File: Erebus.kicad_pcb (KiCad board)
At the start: 2 copper layers, 339.1 x 143.2 mm, 382 parts, among them Q1 BSS138, Q2 BSS138, SW1 SW_SPST, SW10 SLSS49E-3, SW11 SLSS49E-3, SW12 SLSS49E-3, SW13 SLSS49E-3, SW14 SLSS49E-3, SW15 SLSS49E-3, SW16 SLSS49E-3, SW17 SLSS49E-3, SW18 SLSS49E-3, SW19 SLSS49E-3, SW2 SLSS49E-3, SW20 SLSS49E-3, SW21 SLSS49E-3, SW22 SLSS49E-3, SW23 SLSS49E-3, SW24 SLSS49E-3, SW25 SLSS49E-3, SW26 SLSS49E-3, SW27 SLSS49E-3, SW28 SLSS49E-3, SW29 SLSS49E-3, SW3 SLSS49E-3, SW30 SLSS49E-3, SW31 SLSS49E-3, SW32 SLSS49E-3, SW33 SLSS49E-3, SW34 SLSS49E-3, SW35 SLSS49E-3, SW36 SLSS49E-3, SW37 SLSS49E-3, SW38 SLSS49E-3, SW39 SLSS49E-3, SW4 SLSS49E-3, SW40 SLSS49E-3, SW41 SLSS49E-3, SW42 SLSS49E-3, SW43 SLSS49E-3, SW44 SLSS49E-3, SW45 SLSS49E-3, SW46 SLSS49E-3, SW47 SLSS49E-3, SW48 SLSS49E-3, SW49 SLSS49E-3, SW5 SLSS49E-3, SW50 SLSS49E-3, SW51 SLSS49E-3, SW52 SLSS49E-3, SW53 SLSS49E-3, SW54 SLSS49E-3, SW55 SLSS49E-3, SW56 SLSS49E-3, SW57 SLSS49E-3, SW58 SLSS49E-3, SW59 SLSS49E-3, SW6 SLSS49E-3, SW60 SLSS49E-3, SW61 SLSS49E-3, SW62 SLSS49E-3, SW63 SLSS49E-3, SW64 SLSS49E-3, SW65 SLSS49E-3, SW66 SLSS49E-3, SW67 SLSS49E-3, SW68 SLSS49E-3, SW69 SLSS49E-3, SW7 SLSS49E-3, SW70 SLSS49E-3, SW71 SLSS49E-3, SW72 SLSS49E-3, SW73 SLSS49E-3, SW74 SLSS49E-3, SW75 SLSS49E-3, SW76 SLSS49E-3, SW77 SLSS49E-3, SW78 SLSS49E-3, SW79 SLSS49E-3, SW8 SLSS49E-3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

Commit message: Switched to split layout ortholinear
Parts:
- removed C1, C169: 10u, Capacitor_SMD:C_0402_1005Metric
- removed C10, C100, C101, C102, C103, C104, C105, C106, C107, C108, C109, C11, C110, C111, C112, C113, C114, C115, C116, C117, C118, C119, C12, C120, C121, C122, C123, C124, C125, C126, C127, C128, C129, C13, C130, C131, C132, C133, C134, C135, C136, C137, C138, C139, C14, C140, C141, C142, C143, C144, C145, C146, C147, C148, C149, C15, C150, C151, C152, C153, C154, C155, C156, C157, C158, C159, C16, C160, C161, C162, C163, C164, C165, C166, C167, C168, C17, C170, C171, C172, C173, C174, C18, C19, C20, C21, C22, C23, C24, C25, C26, C27, C28, C29, C30, C31, C32, C33, C34, C35, C36, C37, C38, C39, C40, C41, C42, C43, C44, C45, C46, C47, C48, C49, C5, C50, C51, C52, C53, C54, C55, C56, C57, C58, C59, C6, C60, C61, C62, C63, C64, C65, C66, C67, C68, C69, C7, C70, C71, C72, C73, C74, C75, C76, C77, C78, C79, C8, C80, C81, C82, C83, C84, C85, C86, C87, C88, C89, C9, C90, C91, C92, C93, C94, C95, C96, C97, C98, C99: 100n, Capacitor_SMD:C_0402_1005Metric
- removed C2: 100u, Capacitor_SMD:C_0402_1005Metric
- removed C3, C4: 22p, Capacitor_SMD:C_0402_1005Metric
- removed ENCODER1: EC11E, PCM_marbastlib-various:ROT_Alps_EC11E-Switch
- removed H1, H2, H3, H4, H5, H6, H7, H8: MountingHole, MountingHole:MountingHole_2.2mm_M2_Pad
- removed Q1, Q2: BSS138, Package_TO_SOT_SMD:SOT-23
- removed R1, R2: 0, Resistor_SMD:R_0603_1608Metric_Pad0.98x0.95mm_HandSolder
- removed R10, R11, R12, R13, R14, R15, R16, R17, R18, R19, R20, R21, R22, R23, R24, R25, R26, R27, R28, R29, R30, R31, R32, R33, R34, R35, R36, R37, R38, R39, R4, R40, R41, R42, R43, R44, R45, R46, R47, R48, R49, R5, R50, R51, R52, R53, R54, R55, R56, R57, R58, R59, R6, R60, R61, R62, R63, R64, R65, R66, R67, R68, R69, R7, R70, R71, R72, R73, R74, R75, R76, R77, R78, R79, R8, R80, R81, R82, R85, R86, R9, R90, R91, R92: 10k, Resistor_SMD:R_0402_1005Metric
- removed R3: 1k5, Resistor_SMD:R_0402_1005Metric
- removed R83: 330k, Resistor_SMD:R_0603_1608Metric
- removed R84: 1M, Resistor_SMD:R_0402_1005Metric
- removed R87: 100k, Resistor_SMD:R_0402_1005Metric
- removed R88: 100, Resistor_SMD:R_0402_1005Metric
- removed R89: 1k, Resistor_SMD:R_0402_1005Metric
- removed S1, S4: MX_stab, PCM_marbastlib-mx:STAB_MX_P_2u
- removed S2, S3: MX_stab, PCM_marbastlib-mx:STAB_MX_P_2.25u
- removed S5: MX_stab, PCM_marbastlib-mx:STAB_MX_P_2.75u
- removed SW28, SW29, SW30, SW31, SW32, SW33, SW34, SW35, SW36, SW37, SW38, SW39, SW40, SW41, SW42, SW43, SW44, SW45, SW46, SW47, SW48, SW49, SW50, SW51, SW52, SW53, SW54, SW55, SW56, SW57, SW58, SW59, SW60, SW61, SW62, SW63, SW64, SW65, SW66, SW67, SW68, SW69, SW70, SW71, SW72, SW73, SW74, SW75, SW76, SW77, SW78, SW79, SW80, SW81, SW82: SLSS49E-3, Erebus:SLSS49E-3 with MX holes
- removed SWD1: Conn_02x03_Odd_Even, Connector_PinHeader_2.54mm:PinHeader_2x03_P2.54mm_Vertical
- removed U10, U11, U6, U7, U8, U9: 74HC4067, Package_SO:TSSOP-24_4.4x7.8mm_P0.65mm
- removed U2, U3: H5VU25U, Erebus:DFN2510
- removed U4: AT32F415CBT7, easyeda2kicad:LQFP-48_L7.0-W7.0-P0.50-LS9.0-BL
- removed U5: STM32F303CBTx, Package_QFP:LQFP-48_7x7mm_P0.5mm
- removed USB1: X1224WRS-04-LPV01, Erebus:PicoEZMate-Reinforced-Alt
- removed Y1: 8MHz, Crystal:Crystal_SMD_3225-4Pin_3.2x2.5mm
- added BT1: JST Connector, KLOR:JST_PH_reversible, F.Cu at (82.3, 104.8)
- added BT2: Battery_Cell, KLOR:custombatteryconnector_small, F.Cu at (82.5, 113.2)
- added D10: D_Small, KLOR:Diode_SOD123, F.Cu at (193.6, 111.0)
- added D11: D_Small, KLOR:Diode_SOD123, F.Cu at (221.9, 110.9)
- added D12: D_Small, KLOR:Diode_SOD123, F.Cu at (116.8, 118.3)
- added D13: D_Small, KLOR:Diode_SOD123, F.Cu at (148.2, 103.2)
- added D14: D_Small, KLOR:Diode_SOD123, F.Cu at (155.0, 106.3)
- added D15: D_Small, KLOR:Diode_SOD123, F.Cu at (174.6, 116.3)
- added D16: D_Small, KLOR:Diode_SOD123, F.Cu at (190.3, 129.7)
- added D17: D_Small, KLOR:Diode_SOD123, F.Cu at (218.5, 129.5)
- added D18: D_Small, KLOR:Diode_SOD123, F.Cu at (100.9, 107.0)
- added D19: D_Small, KLOR:Diode_SOD123, F.Cu at (88.3, 143.7)
- added D2: D_Small, KLOR:Diode_SOD123, F.Cu at (136.0, 77.1)
- added D20: D_Small, KLOR:Diode_SOD123, F.Cu at (107.5, 131.9)
- added D21: D_Small, KLOR:Diode_SOD123, F.Cu at (129.1, 125.2)
- added D22: D_Small, KLOR:Diode_SOD123, F.Cu at (151.6, 124.3)
- added D3: D_Small, KLOR:Diode_SOD123, F.Cu at (155.1, 68.1)
- added D4: D_Small, KLOR:Diode_SOD123, F.Cu at (176.0, 78.2)
- added D5: D_Small, KLOR:Diode_SOD123, F.Cu at (196.9, 92.2)
- added D6: D_Small, KLOR:Diode_SOD123, F.Cu at (117.0, 99.2)
- added D7: D_Small, KLOR:Diode_SOD123, F.Cu at (137.0, 96.2)
- added D8: D_Small, KLOR:Diode_SOD123, F.Cu at (155.1, 87.2)
- added D9: D_Small, KLOR:Diode_SOD123, F.Cu at (174.6, 97.3)
- added J1: MJ-4PP-9, KLOR:MJ-4PP-9, F.Cu at (80.9, 127.4)
- added JP22: Device_Jumper_NO_Small, KLOR:Jumper, F.Cu at (81.9, 108.5)
- added JP23: Device_Jumper_NO_Small, KLOR:Jumper, B.Cu at (83.7, 108.5)
- added JP24: Device_Jumper_NO_Small, KLOR:Jumper, F.Cu at (83.7, 108.5)
- added JP25: Device_Jumper_NO_Small, KLOR:Jumper, B.Cu at (81.9, 108.5)
- added JP26: Device_Jumper_NO_Small, KLOR:Jumper, B.Cu at (91.0, 136.6)
- added JP3: Device_Jumper_NO_Small, KLOR:Jumper, F.Cu at (95.2, 101.8)
- added JP4: Device_Jumper_NO_Small, KLOR:Jumper, F.Cu at (92.6, 101.8)
- added JP5: Device_Jumper_NO_Small, KLOR:Jumper, B.Cu at (100.2, 101.8)
- added JP6: Device_Jumper_NO_Small, KLOR:Jumper, B.Cu at (97.7, 101.8)
- added JP7: Device_Jumper_NO_Small, KLOR:Jumper, B.Cu at (95.2, 101.8)
- added JP8: Device_Jumper_NO_Small, KLOR:Jumper, B.Cu at (92.6, 101.8)
- added MH1: MountingHole_3.2mm_M3, MountingHole:MountingHole_3.2mm_M3, F.Cu at (83.3, 36.6)
- added MH2: MountingHole_3.2mm_M3, MountingHole:MountingHole_3.2mm_M3, F.Cu at (145.4, 36.6)
- added MH3: MountingHole_3.2mm_M3, MountingHole:MountingHole_3.2mm_M3, F.Cu at (175.5, 36.7)
- added MH4: MountingHole_3.2mm_M3, MountingHole:MountingHole_3.2mm_M3, F.Cu at (190.3, 37.7)
- added MH5: MountingHole_3.2mm_M3, MountingHole:MountingHole_3.2mm_M3, F.Cu at (167.3, 88.0)
- added MH6: MountingHole_3.2mm_M3, MountingHole:MountingHole_3.2mm_M3, F.Cu at (83.3, 135.2)
- added MH7: MountingHole_3.2mm_M3, MountingHole:MountingHole_3.2mm_M3, F.Cu at (169.9, 121.7)
- added MH8: MountingHole_3.2mm_M3, MountingHole:MountingHole_3.2mm_M3, F.Cu at (181.6, 122.5)
- added MH9: MountingHole_2.2mm_M2, MountingHole:MountingHole_2.2mm_M2, F.Cu at (196.6, 56.3)
- added PSW1: SW_DPDT_x2, KLOR:MSK12C02_reversible, F.Cu at (80.9, 41.1)
- added RSW1: SW_Push, KLOR:SW_Push_1P1T-MP_NO_Horizontal_Alps_SKRTLAE010_both_sides, F.Cu at (82.3, 120.7)
- D1: value 1N4148WS -> D_Small; footprint Diode_SMD:D_SOD-323 -> KLOR:Diode_SOD123
- JP1, JP2: value Jumper_2_Open -> Device_Jumper_NO_Small; footprint Connector_PinHeader_2.54mm:PinHeader_1x02_P2.54mm_Vertical -> KLOR:Jumper
- OLED1: value Conn_01x04_Socket -> SSD1306; footprint Erebus:OLED Module -> KLOR:SSD1306_128x64OLED
- SW1: value SW_SPST -> SW_PUSH-MX_W_LED; footprint Button_Switch_SMD:SW_SPST_TL3342 -> KLOR:SK6812MINI_and_cherry; moved to F.Cu
- SW10, SW11, SW12, SW13, SW14, SW15, SW16, SW17, SW19, SW2, SW20, SW21, SW22, SW23, SW24, SW25, SW26, SW27, SW3, SW4, SW5, SW6, SW7, SW8, SW9: value SLSS49E-3 -> SW_PUSH-MX_W_LED; footprint Erebus:SLSS49E-3 with MX holes -> KLOR:SK6812MINI_and_cherry; moved to F.Cu
- SW18: value SLSS49E-3 -> RotaryEncoder_Switch; footprint Erebus:SLSS49E-3 with MX holes -> KLOR:RotaryEncoder_Alps_EC11E-Switch_Vertical_H20mm-keebio_modified; moved to F.Cu
- U1: value AMS1117-3.3 -> ProMicro; footprint Package_TO_SOT_SMD:SOT-223-3_TabPin2 -> KLOR:ProMicro
- moved D1 293.0 mm to (117.0, 80.1)
- moved U1 293.0 mm to (97.6, 52.5)
- moved SW15 185.5 mm to (178.2, 108.1), turned to 176 degrees
- moved SW13 154.8 mm to (140.1, 106.7)
- moved SW12 153.3 mm to (121.1, 109.7), turned to 180 degrees
- moved SW16 151.8 mm to (196.1, 122.1), turned to 170 degrees
- moved SW17 151.7 mm to (215.7, 120.5), turned to 170 degrees
- moved SW14 151.1 mm to (159.1, 97.7)
- moved SW5 102.6 mm to (202.7, 84.5), turned to 170 degrees
- moved SW2 98.4 mm to (140.1, 68.6)
- moved SW4 97.2 mm to (180.9, 70.0), turned to 176 degrees
- moved SW3 91.7 mm to (159.1, 59.6)
- moved SW19 90.9 mm to (85.4, 152.9), turned to -135 degrees
- moved OLED1 89.1 mm to (96.6, 87.9), turned to 180 degrees
- moved JP2 83.3 mm to (97.7, 101.8), turned to -90 degrees
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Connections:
- D1 pad 1: Net-(D1-K) -> row0
- D1 pad 2: /reset/switch -> Net-(D1-A)
- JP1 pad 1: GND -> Net-(OLED1-GND)
- JP1 pad 2: /~{RESET} -> GND
- JP2 pad 1: +3V3 -> Net-(OLED1-VCC)
- JP2 pad 2: /BOOT0 -> VCC
- OLED1 pad 1: GND -> Net-(OLED1-GND)
- OLED1 pad 2: +3V3 -> Net-(OLED1-VCC)
- OLED1 pad 3: /I2C1_SCL -> Net-(OLED1-SCL)
- OLED1 pad 4: /I2C1_SDA -> Net-(OLED1-SDA)
- SW1 pad 1: +3V3 -> Net-(SW1B-DOUT)
- SW1 pad 2: /reset/switch -> GND
- SW10 pad 1: +3V3 -> Net-(SW10B-DOUT)
- SW10 pad 3: Net-(SW10-VOUT) -> Net-(SW10B-DIN)
- SW11 pad 1: +3V3 -> Net-(SW11B-DOUT)
- SW11 pad 3: Net-(SW11-VOUT) -> Net-(SW11B-DIN)
- SW12 pad 1: +3V3 -> Net-(SW12B-DOUT)
- SW12 pad 3: Net-(SW12-VOUT) -> Net-(SW12B-DIN)
- SW13 pad 1: +3V3 -> Net-(SW13B-DOUT)
- SW13 pad 3: Net-(SW13-VOUT) -> Net-(SW13B-DIN)
- SW14 pad 1: +3V3 -> Net-(SW14B-DOUT)
- SW14 pad 3: Net-(SW14-VOUT) -> Net-(SW14B-DIN)
- SW15 pad 1: +3V3 -> Net-(SW15B-DOUT)
- SW15 pad 3: Net-(SW15-VOUT) -> Net-(SW15B-DIN)
- SW16 pad 1: +3V3 -> Net-(SW10B-DIN)
- SW16 pad 3: Net-(SW16-VOUT) -> Net-(SW15B-DOUT)
- SW17 pad 1: +3V3 -> unconnected-(SW17B-DOUT-Pad1)
- SW17 pad 3: Net-(SW17-VOUT) -> Net-(SW11B-DOUT)
- SW19 pad 1: +3V3 -> Net-(SW19B-DOUT)
- SW19 pad 3: Net-(SW19-VOUT) -> LED
- SW2 pad 1: +3V3 -> Net-(SW2B-DOUT)
- SW2 pad 3: Net-(SW2-VOUT) -> Net-(SW1B-DOUT)
- SW20 pad 1: +3V3 -> Net-(SW20B-DOUT)
- SW20 pad 3: Net-(SW20-VOUT) -> Net-(SW19B-DOUT)
- SW21 pad 1: +3V3 -> Net-(SW12B-DIN)
- SW21 pad 3: Net-(SW21-VOUT) -> Net-(SW20B-DOUT)
- SW22 pad 1: +3V3 -> Net-(SW14B-DIN)
- SW22 pad 3: Net-(SW22-VOUT) -> Net-(SW13B-DOUT)
- SW23 pad 1: +3V3 -> (no net)
- SW23 pad 2: GND -> (no net)
- SW23 pad 3: Net-(SW23-VOUT) -> (no net)
- SW24 pad 1: +3V3 -> (no net)
- SW24 pad 2: GND -> (no net)
- SW24 pad 3: Net-(SW24-VOUT) -> (no net)
- SW25 pad 1: +3V3 -> (no net)
- SW25 pad 2: GND -> (no net)
- SW25 pad 3: Net-(SW25-VOUT) -> (no net)
- SW26 pad 1: +3V3 -> (no net)
- SW26 pad 2: GND -> (no net)
- SW26 pad 3: Net-(SW26-VOUT) -> (no net)
- SW27 pad 1: +3V3 -> (no net)
- SW27 pad 2: GND -> (no net)
- SW27 pad 3: Net-(SW27-VOUT) -> (no net)
- SW3 pad 1: +3V3 -> Net-(SW3B-DOUT)
- SW3 pad 3: Net-(SW3-VOUT) -> Net-(SW3B-DIN)
- SW4 pad 1: +3V3 -> Net-(SW4B-DOUT)
- SW4 pad 3: Net-(SW4-VOUT) -> Net-(SW3B-DOUT)
- SW5 pad 1: +3V3 -> Net-(SW11B-DIN)
- SW5 pad 3: Net-(SW5-VOUT) -> Net-(SW10B-DOUT)
- SW6 pad 1: +3V3 -> Net-(SW1B-DIN)
- SW6 pad 3: Net-(SW6-VOUT) -> Net-(SW12B-DOUT)
- SW7 pad 1: +3V3 -> Net-(SW13B-DIN)
- SW7 pad 3: Net-(SW7-VOUT) -> Net-(SW2B-DOUT)
- SW8 pad 1: +3V3 -> Net-(SW3B-DIN)
- SW8 pad 3: Net-(SW8-VOUT) -> Net-(SW14B-DOUT)
- SW9 pad 1: +3V3 -> Net-(SW15B-DIN)
- SW9 pad 3: Net-(SW9-VOUT) -> Net-(SW4B-DOUT)
- U1 pad 1: GND -> LED
- U1 pad 2: +3V3 -> TX
- U1 pad 3: +5V -> GND
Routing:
- net GND: track 343.4 -> 0.00 mm, vias 248 -> 0
- net /S0: track 290.4 -> 0.00 mm
- net /S2: track 287.0 -> 0.00 mm
- net /S1: track 286.8 -> 0.00 mm
- net /S3: track 279.9 -> 0.00 mm
- net /ENCODER_B: track 182.5 -> 0.00 mm
- net /ENCODER_A: track 176.6 -> 0.00 mm
- net /ENCODER_SW: track 173.4 -> 0.00 mm
- net /ADC1_IN3: track 149.6 -> 0.00 mm
- net +3V3: track 110.1 -> 0.00 mm
- net /multiplexers/keys/KEYS_0_13: track 88.7 -> 0.00 mm, vias 2 -> 0
- net /multiplexers/keys/KEYS_0_10: track 82.9 -> 0.00 mm, vias 2 -> 0
- net /multiplexers/keys/KEYS_0_12: track 79.2 -> 0.00 mm, vias 2 -> 0
- net /multiplexers/keys/KEYS_0_8: track 79.0 -> 0.00 mm, vias 2 -> 0
- net /multiplexers/keys/KEYS_0_2: track 73.0 -> 0.00 mm, vias 2 -> 0
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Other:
- board size 339.1 x 143.2 mm -> 160 x 137.3 mm
- rule pad_to_mask_clearance: 0.038 -> 0
- board text added: "--AUDIO"
- board text added: "--GND"
- board text added: "--LED"
- board text added: "--ROW0"
- board text added: "--ROW1"
- board text added: "--ROW2"
- board text added: "--ROW3"
- board text added: "--RX"
- board text added: "--SCL"
- board text added: "--SDA"
- board text added: "--TX"
- board text added: "BATT"
- board text added: "BATT+--"
- board text added: "BLK"
- board text added: "COL0--"
- board text added: "COL1--"
- board text added: "COL2--"
- board text added: "COL3--"
- board text added: "COL4--"
- board text added: "COL5--"
- board text added: "ENC"
- board text added: "ENC A--"
- board text added: "ENC B--"
- board text added: "GND"
- board text added: "GND--"
- board text added: "LOST THUMB?"
- board text added: "MOUNT MCU ON BOTTOM COMPONENTS FACING PCB"
- board text added: "OLED"
- board text added: "RED"
- board text added: "RST"
- board text added: "RST--"
- board text added: "SCL"
- board text added: "SDA"
- board text added: "TENTING PUCK"
- board text added: "TRACK BALL"
- board text added: "VCC"
- board text added: "VCC--"

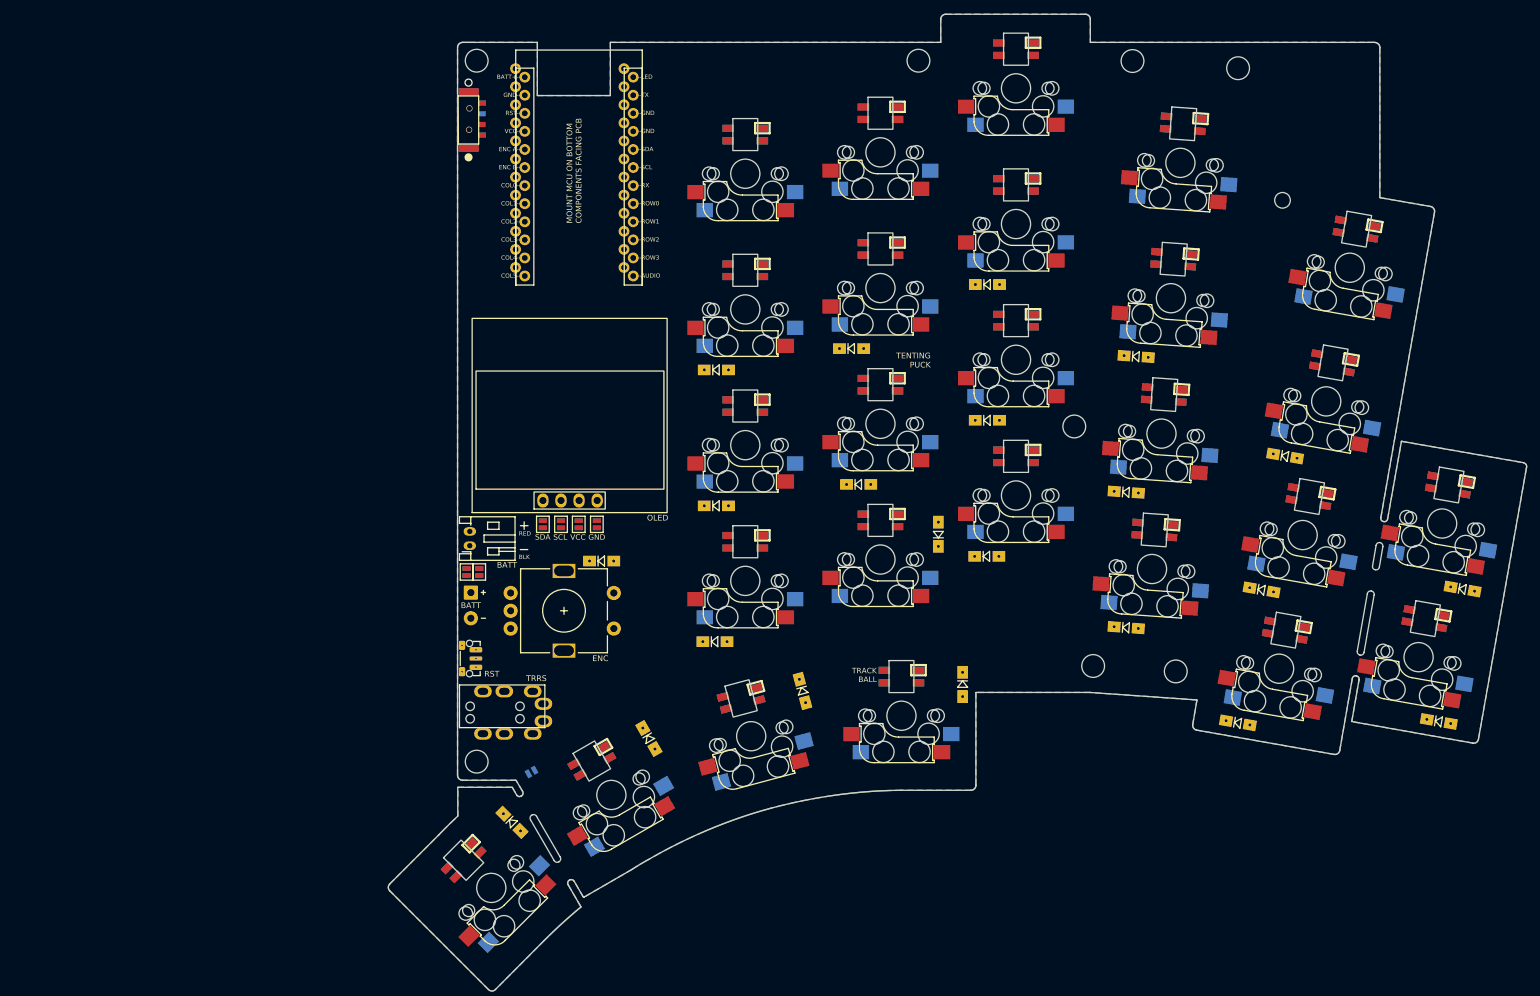
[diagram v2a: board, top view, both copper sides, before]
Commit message: Added and finalized layout of switches
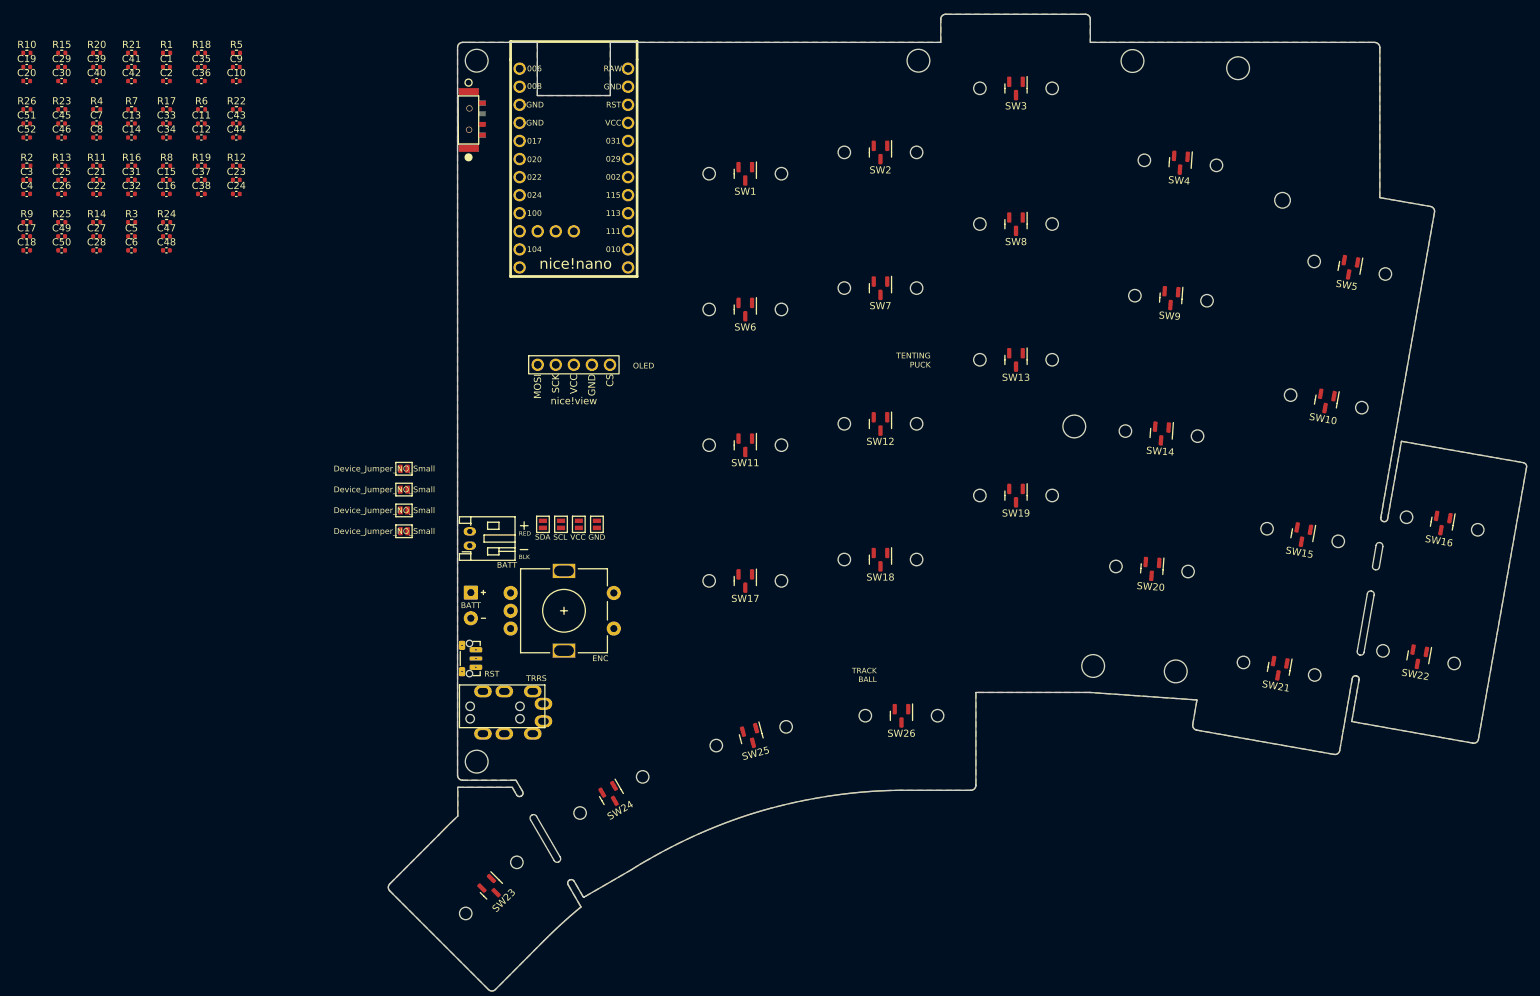
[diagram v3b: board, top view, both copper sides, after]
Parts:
- removed D1, D10, D11, D12, D13, D14, D15, D16, D17, D18, D19, D2, D20, D21, D22, D3, D4, D5, D6, D7, D8, D9: D_Small, KLOR:Diode_SOD123
- removed JP22, JP23, JP24, JP25, JP26: Device_Jumper_NO_Small, KLOR:Jumper
- removed OLED1: SSD1306, KLOR:SSD1306_128x64OLED
- removed SW27: SW_PUSH-MX_W_LED, KLOR:SK6812MINI_and_cherry
- added C1: 100n, Capacitor_SMD:C_0402_1005Metric, F.Cu at (39.7, 37.5)
- added C10: 100n, Capacitor_SMD:C_0402_1005Metric, F.Cu at (49.5, 39.5)
- added C11: 100n, Capacitor_SMD:C_0402_1005Metric, F.Cu at (44.6, 45.5)
- added C12: 100n, Capacitor_SMD:C_0402_1005Metric, F.Cu at (44.6, 47.4)
- added C13: 100n, Capacitor_SMD:C_0402_1005Metric, F.Cu at (34.8, 45.5)
- added C14: 100n, Capacitor_SMD:C_0402_1005Metric, F.Cu at (34.8, 47.4)
- added C15: 100n, Capacitor_SMD:C_0402_1005Metric, F.Cu at (39.7, 53.4)
- added C16: 100n, Capacitor_SMD:C_0402_1005Metric, F.Cu at (39.7, 55.4)
- added C17: 100n, Capacitor_SMD:C_0402_1005Metric, F.Cu at (20.1, 61.3)
- added C18: 100n, Capacitor_SMD:C_0402_1005Metric, F.Cu at (20.1, 63.3)
- added C19: 100n, Capacitor_SMD:C_0402_1005Metric, F.Cu at (20.1, 37.5)
- added C2: 100n, Capacitor_SMD:C_0402_1005Metric, F.Cu at (39.7, 39.5)
- added C20: 100n, Capacitor_SMD:C_0402_1005Metric, F.Cu at (20.1, 39.5)
- added C21: 100n, Capacitor_SMD:C_0402_1005Metric, F.Cu at (29.9, 53.4)
- added C22: 100n, Capacitor_SMD:C_0402_1005Metric, F.Cu at (29.9, 55.4)
- added C23: 100n, Capacitor_SMD:C_0402_1005Metric, F.Cu at (49.5, 53.4)
- added C24: 100n, Capacitor_SMD:C_0402_1005Metric, F.Cu at (49.5, 55.4)
- added C25: 100n, Capacitor_SMD:C_0402_1005Metric, F.Cu at (25.0, 53.4)
- added C26: 100n, Capacitor_SMD:C_0402_1005Metric, F.Cu at (25.0, 55.4)
- added C27: 100n, Capacitor_SMD:C_0402_1005Metric, F.Cu at (29.9, 61.3)
- added C28: 100n, Capacitor_SMD:C_0402_1005Metric, F.Cu at (29.9, 63.3)
- added C29: 100n, Capacitor_SMD:C_0402_1005Metric, F.Cu at (25.0, 37.5)
- added C3: 100n, Capacitor_SMD:C_0402_1005Metric, F.Cu at (20.1, 53.4)
- added C30: 100n, Capacitor_SMD:C_0402_1005Metric, F.Cu at (25.0, 39.5)
- added C31: 100n, Capacitor_SMD:C_0402_1005Metric, F.Cu at (34.8, 53.4)
- added C32: 100n, Capacitor_SMD:C_0402_1005Metric, F.Cu at (34.8, 55.4)
- added C33: 100n, Capacitor_SMD:C_0402_1005Metric, F.Cu at (39.7, 45.5)
- added C34: 100n, Capacitor_SMD:C_0402_1005Metric, F.Cu at (39.7, 47.4)
- added C35: 100n, Capacitor_SMD:C_0402_1005Metric, F.Cu at (44.6, 37.5)
- added C36: 100n, Capacitor_SMD:C_0402_1005Metric, F.Cu at (44.6, 39.5)
- added C37: 100n, Capacitor_SMD:C_0402_1005Metric, F.Cu at (44.6, 53.4)
- added C38: 100n, Capacitor_SMD:C_0402_1005Metric, F.Cu at (44.6, 55.4)
- added C39: 100n, Capacitor_SMD:C_0402_1005Metric, F.Cu at (29.9, 37.5)
- added C4: 100n, Capacitor_SMD:C_0402_1005Metric, F.Cu at (20.1, 55.4)
- added C40: 100n, Capacitor_SMD:C_0402_1005Metric, F.Cu at (29.9, 39.5)
- added C41: 100n, Capacitor_SMD:C_0402_1005Metric, F.Cu at (34.8, 37.5)
- added C42: 100n, Capacitor_SMD:C_0402_1005Metric, F.Cu at (34.8, 39.5)
- added C43: 100n, Capacitor_SMD:C_0402_1005Metric, F.Cu at (49.5, 45.5)
- added C44: 100n, Capacitor_SMD:C_0402_1005Metric, F.Cu at (49.5, 47.4)
- added C45: 100n, Capacitor_SMD:C_0402_1005Metric, F.Cu at (25.0, 45.5)
- added C46: 100n, Capacitor_SMD:C_0402_1005Metric, F.Cu at (25.0, 47.4)
- added C47: 100n, Capacitor_SMD:C_0402_1005Metric, F.Cu at (39.7, 61.3)
- added C48: 100n, Capacitor_SMD:C_0402_1005Metric, F.Cu at (39.7, 63.3)
- added C49: 100n, Capacitor_SMD:C_0402_1005Metric, F.Cu at (25.0, 61.3)
- added C5: 100n, Capacitor_SMD:C_0402_1005Metric, F.Cu at (34.8, 61.3)
- added C50: 100n, Capacitor_SMD:C_0402_1005Metric, F.Cu at (25.0, 63.3)
- added C51: 100n, Capacitor_SMD:C_0402_1005Metric, F.Cu at (20.1, 45.5)
- added C52: 100n, Capacitor_SMD:C_0402_1005Metric, F.Cu at (20.1, 47.4)
- added C6: 100n, Capacitor_SMD:C_0402_1005Metric, F.Cu at (34.8, 63.3)
- added C7: 100n, Capacitor_SMD:C_0402_1005Metric, F.Cu at (29.9, 45.5)
- added C8: 100n, Capacitor_SMD:C_0402_1005Metric, F.Cu at (29.9, 47.4)
- added C9: 100n, Capacitor_SMD:C_0402_1005Metric, F.Cu at (49.5, 37.5)
- added Display1: nice!view, EREBUS:nice_view, F.Cu at (97.0, 62.9)
- added ENCODER1: RotaryEncoder_Switch, EREBUS:RotaryEncoder_Alps_EC11E-Switch_Vertical_H20mm-keebio_modified, F.Cu at (95.6, 114.0)
- added R1: 10k, Resistor_SMD:R_0402_1005Metric, F.Cu at (39.7, 35.6)
- added R10: 10k, Resistor_SMD:R_0402_1005Metric, F.Cu at (20.1, 35.6)
- added R11: 10k, Resistor_SMD:R_0402_1005Metric, F.Cu at (29.9, 51.4)
- added R12: 10k, Resistor_SMD:R_0402_1005Metric, F.Cu at (49.6, 51.4)
- added R13: 10k, Resistor_SMD:R_0402_1005Metric, F.Cu at (25.0, 51.4)
- added R14: 10k, Resistor_SMD:R_0402_1005Metric, F.Cu at (29.9, 59.4)
- added R15: 10k, Resistor_SMD:R_0402_1005Metric, F.Cu at (25.0, 35.6)
- added R16: 10k, Resistor_SMD:R_0402_1005Metric, F.Cu at (34.8, 51.4)
- added R17: 10k, Resistor_SMD:R_0402_1005Metric, F.Cu at (39.7, 43.5)
- added R18: 10k, Resistor_SMD:R_0402_1005Metric, F.Cu at (44.6, 35.6)
- added R19: 10k, Resistor_SMD:R_0402_1005Metric, F.Cu at (44.6, 51.4)
- added R2: 10k, Resistor_SMD:R_0402_1005Metric, F.Cu at (20.1, 51.4)
- added R20: 10k, Resistor_SMD:R_0402_1005Metric, F.Cu at (29.9, 35.6)
- added R21: 10k, Resistor_SMD:R_0402_1005Metric, F.Cu at (34.8, 35.6)
- added R22: 10k, Resistor_SMD:R_0402_1005Metric, F.Cu at (49.6, 43.5)
- added R23: 10k, Resistor_SMD:R_0402_1005Metric, F.Cu at (25.0, 43.5)
- added R24: 10k, Resistor_SMD:R_0402_1005Metric, F.Cu at (39.7, 59.4)
- added R25: 10k, Resistor_SMD:R_0402_1005Metric, F.Cu at (25.0, 59.4)
- added R26: 10k, Resistor_SMD:R_0402_1005Metric, F.Cu at (20.1, 43.5)
- added R3: 10k, Resistor_SMD:R_0402_1005Metric, F.Cu at (34.8, 59.4)
- added R4: 10k, Resistor_SMD:R_0402_1005Metric, F.Cu at (29.9, 43.5)
- added R5: 10k, Resistor_SMD:R_0402_1005Metric, F.Cu at (49.6, 35.6)
- added R6: 10k, Resistor_SMD:R_0402_1005Metric, F.Cu at (44.6, 43.5)
- added R7: 10k, Resistor_SMD:R_0402_1005Metric, F.Cu at (34.8, 43.5)
- added R8: 10k, Resistor_SMD:R_0402_1005Metric, F.Cu at (39.7, 51.4)
- added R9: 10k, Resistor_SMD:R_0402_1005Metric, F.Cu at (20.1, 59.4)
- BT1: value JST Connector -> Battery_Cell
- BT2: value Battery_Cell -> JST Connector
- JP1, JP2, JP3, JP4: footprint KLOR:Jumper -> EREBUS:Jumper
- JP5, JP6, JP7, JP8: moved to F.Cu
- SW1, SW10, SW11, SW12, SW13, SW14, SW15, SW16, SW17, SW19, SW2, SW20, SW21, SW22, SW23, SW24, SW25, SW26, SW3, SW4, SW5, SW6, SW7, SW8, SW9: value SW_PUSH-MX_W_LED -> SLSS49E-3; footprint KLOR:SK6812MINI_and_cherry -> EREBUS:SLSS49E-3 with MX holes
- SW18: value RotaryEncoder_Switch -> SLSS49E-3; footprint KLOR:RotaryEncoder_Alps_EC11E-Switch_Vertical_H20mm-keebio_modified -> EREBUS:SLSS49E-3 with MX holes
- U1: value ProMicro -> nice_nano; footprint KLOR:ProMicro -> EREBUS:nice_nano
- moved SW23 106.5 mm to (85.4, 152.9), turned to 45 degrees
- moved SW11 98.5 mm to (121.1, 90.7), turned to 0 degrees
- moved SW25 98.4 mm to (121.9, 131.6), turned to 15 degrees
- moved SW24 97.9 mm to (102.2, 139.8), turned to 30 degrees
- moved SW17 95.2 mm to (121.1, 109.7), turned to 0 degrees
- moved SW19 92.1 mm to (159.1, 97.7), turned to 0 degrees
- moved SW26 87.0 mm to (143.0, 128.7), turned to 0 degrees
- moved SW20 82.3 mm to (178.2, 108.1), turned to -4 degrees
- moved SW21 74.8 mm to (196.1, 122.1), turned to -10 degrees
- moved SW22 73.1 mm to (215.7, 120.5), turned to -10 degrees
- moved SW18 45.1 mm to (140.1, 106.7)
- moved SW13 33.9 mm to (159.1, 78.7), turned to 0 degrees
- moved SW16 30.7 mm to (219.0, 101.7), turned to -10 degrees
- moved SW12 29.1 mm to (140.1, 87.7), turned to 0 degrees
- moved JP1 28.2 mm to (73.1, 94.0), turned to 0 degrees
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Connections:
- BT1 pad 1: /PAD1 -> /PSW
- BT1 pad 2: /PAD2 -> GND
- BT2 pad 1: /PSW -> /PAD1
- BT2 pad 2: GND -> /PAD2
- JP1 pad 1: Net-(OLED1-GND) -> /PAD2
- JP1 pad 2: GND -> /PSW
- JP2 pad 1: Net-(OLED1-VCC) -> /PAD2
- JP2 pad 2: VCC -> GND
- JP3 pad 1: Net-(OLED1-SCL) -> /PAD1
- JP3 pad 2: SCL -> GND
- JP4 pad 1: Net-(OLED1-SDA) -> /PAD1
- JP4 pad 2: SDA -> /PSW
- JP5 pad 1: Net-(OLED1-GND) -> Net-(Display1-GND)
- JP5 pad 2: SDA -> GND
- JP6 pad 1: Net-(OLED1-VCC) -> Net-(Display1-VCC)
- JP6 pad 2: SCL -> VCC
- JP7 pad 1: Net-(OLED1-SCL) -> Net-(Display1-SCK)
- JP7 pad 2: VCC -> SCL
- JP8 pad 1: Net-(OLED1-SDA) -> Net-(Display1-MOSI)
- JP8 pad 2: GND -> SDA
- SW1 pad 1: Net-(SW1B-DOUT) -> +3V3
- SW1 pad 3: Net-(SW1B-DIN) -> Net-(SW1-VOUT)
- SW10 pad 1: Net-(SW10B-DOUT) -> +3V3
- SW10 pad 3: Net-(SW10B-DIN) -> Net-(SW10-VOUT)
- SW11 pad 1: Net-(SW11B-DOUT) -> +3V3
- SW11 pad 3: Net-(SW11B-DIN) -> Net-(SW11-VOUT)
- SW12 pad 1: Net-(SW12B-DOUT) -> +3V3
- SW12 pad 3: Net-(SW12B-DIN) -> Net-(SW12-VOUT)
- SW13 pad 1: Net-(SW13B-DOUT) -> +3V3
- SW13 pad 3: Net-(SW13B-DIN) -> Net-(SW13-VOUT)
- SW14 pad 1: Net-(SW14B-DOUT) -> +3V3
- SW14 pad 3: Net-(SW14B-DIN) -> Net-(SW14-VOUT)
- SW15 pad 1: Net-(SW15B-DOUT) -> +3V3
- SW15 pad 3: Net-(SW15B-DIN) -> Net-(SW15-VOUT)
- SW16 pad 1: Net-(SW10B-DIN) -> +3V3
- SW16 pad 3: Net-(SW15B-DOUT) -> Net-(SW16-VOUT)
- SW17 pad 1: unconnected-(SW17B-DOUT-Pad1) -> +3V3
- SW17 pad 3: Net-(SW11B-DOUT) -> Net-(SW17-VOUT)
- SW19 pad 1: Net-(SW19B-DOUT) -> +3V3
- SW19 pad 3: LED -> Net-(SW19-VOUT)
- SW2 pad 1: Net-(SW2B-DOUT) -> +3V3
- SW2 pad 3: Net-(SW1B-DOUT) -> Net-(SW2-VOUT)
- SW20 pad 1: Net-(SW20B-DOUT) -> +3V3
- SW20 pad 3: Net-(SW19B-DOUT) -> Net-(SW20-VOUT)
- SW21 pad 1: Net-(SW12B-DIN) -> +3V3
- SW21 pad 3: Net-(SW20B-DOUT) -> Net-(SW21-VOUT)
- SW22 pad 1: Net-(SW14B-DIN) -> +3V3
- SW22 pad 3: Net-(SW13B-DOUT) -> Net-(SW22-VOUT)
- SW23 pad 1: (no net) -> +3V3
- SW23 pad 2: (no net) -> GND
- SW23 pad 3: (no net) -> Net-(SW23-VOUT)
- SW24 pad 1: (no net) -> +3V3
- SW24 pad 2: (no net) -> GND
- SW24 pad 3: (no net) -> Net-(SW24-VOUT)
- SW25 pad 1: (no net) -> +3V3
- SW25 pad 2: (no net) -> GND
- SW25 pad 3: (no net) -> Net-(SW25-VOUT)
- SW26 pad 1: (no net) -> +3V3
- SW26 pad 2: (no net) -> GND
- SW26 pad 3: (no net) -> Net-(SW26-VOUT)
- SW3 pad 1: Net-(SW3B-DOUT) -> +3V3
- SW3 pad 3: Net-(SW3B-DIN) -> Net-(SW3-VOUT)
- SW4 pad 1: Net-(SW4B-DOUT) -> +3V3
- SW4 pad 3: Net-(SW3B-DOUT) -> Net-(SW4-VOUT)
- SW5 pad 1: Net-(SW11B-DIN) -> +3V3
- SW5 pad 3: Net-(SW10B-DOUT) -> Net-(SW5-VOUT)
- SW6 pad 1: Net-(SW1B-DIN) -> +3V3
- SW6 pad 3: Net-(SW12B-DOUT) -> Net-(SW6-VOUT)
- SW7 pad 1: Net-(SW13B-DIN) -> +3V3
- SW7 pad 3: Net-(SW2B-DOUT) -> Net-(SW7-VOUT)
- SW8 pad 1: Net-(SW3B-DIN) -> +3V3
- SW8 pad 3: Net-(SW14B-DOUT) -> Net-(SW8-VOUT)
- SW9 pad 1: Net-(SW15B-DIN) -> +3V3
- SW9 pad 3: Net-(SW4B-DOUT) -> Net-(SW9-VOUT)
- U1 pad 1: LED -> unconnected-(U1-TX0/P0.06-Pad1)
- U1 pad 10: row2 -> unconnected-(U1-P0.11-Pad10)
- U1 pad 11: row3 -> unconnected-(U1-P1.04-Pad11)
- U1 pad 12: AUDIO -> unconnected-(U1-P1.06-Pad12)
- U1 pad 13: SW18A -> unconnected-(U1-NFC1/P0.09-Pad13)
- U1 pad 14: col4 -> unconnected-(U1-NFC2/P0.10-Pad14)
- U1 pad 15: col3 -> unconnected-(U1-P1.11-Pad15)
- U1 pad 16: col2 -> unconnected-(U1-P1.13-Pad16)
- U1 pad 17: col1 -> unconnected-(U1-P1.15-Pad17)
- U1 pad 18: col0 -> unconnected-(U1-AIN0/P0.02-Pad18)
- U1 pad 19: ENCB -> unconnected-(U1-AIN5/P0.29-Pad19)
- U1 pad 20: ENCA -> unconnected-(U1-AIN7/P0.31-Pad20)
- U1 pad 3: GND -> unconnected-(U1-GND-Pad3)
- U1 pad 4: GND -> unconnected-(U1-GND-Pad4)
- U1 pad 5: SDA -> unconnected-(U1-P0.17-Pad5)
- U1 pad 6: SCL -> unconnected-(U1-P0.20-Pad6)
- U1 pad 8: row0 -> unconnected-(U1-P0.24-Pad8)
- U1 pad 9: row1 -> unconnected-(U1-P1.00-Pad9)
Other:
- board text removed: "--AUDIO"
- board text removed: "--GND"
- board text removed: "--LED"
- board text removed: "--ROW0"
- board text removed: "--ROW1"
- board text removed: "--ROW2"
- board text removed: "--ROW3"
- board text removed: "--RX"
- board text removed: "--SCL"
- board text removed: "--SDA"
- board text removed: "--TX"
- board text removed: "BATT+--"
- board text removed: "COL0--"
- board text removed: "COL1--"
- board text removed: "COL2--"
- board text removed: "COL3--"
- board text removed: "COL4--"
- board text removed: "COL5--"
- board text removed: "ENC A--"
- board text removed: "ENC B--"
- board text removed: "GND--"
- board text removed: "MOUNT MCU ON BOTTOM COMPONENTS FACING PCB"
- board text removed: "RST--"
- board text removed: "VCC--"
